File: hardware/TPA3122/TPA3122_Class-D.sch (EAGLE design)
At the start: 49 parts, among them CN1 Left_Speaker, CN2 Right_Speaker, CN3 Power_Supply, J1 SJ-3523-SMT, J4 POWER_JACKSLT, Q1 FQP47P06, U1 TPA3122D2_N_20

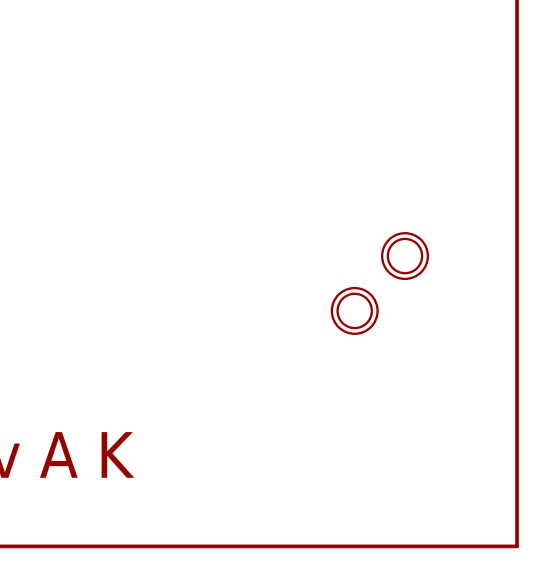
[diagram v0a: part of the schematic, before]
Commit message: Corrected TPA3122 Power Jack
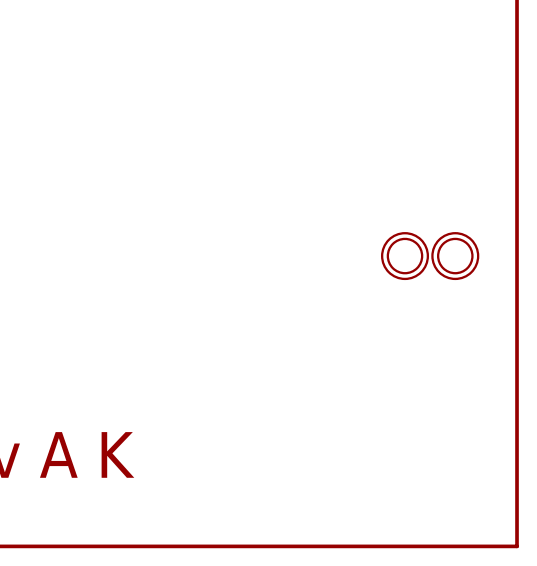
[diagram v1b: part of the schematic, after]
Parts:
- J4: device SparkFun-Connectors:POWER_JACKSLT -> TPA3122:POWER_JACKSLT
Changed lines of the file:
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@@
 <?xml version="1.0" encoding="utf-8"?>
 <!DOCTYPE eagle SYSTEM "eagle.dtd">
-<eagle version="8.4.0">
+<eagle version="8.7.1">
 <drawing>
 <settings>
@@
 <part name="ROUT" library="tlv" library_urn="urn:adsk.eagle:library:1326846" deviceset="TP" device="B2,54" package3d_urn="urn:adsk.eagle:package:1326893/1"/>
 <part name="R_FIL" library="tlv" library_urn="urn:adsk.eagle:library:1326846" deviceset="TP" device="B2,54" package3d_urn="urn:adsk.eagle:package:1326893/1"/>
-<part name="J4" library="SparkFun-Connectors" deviceset="POWER_JACK" device="SLT"/>
+<part name="J4" library="TPA3122" deviceset="POWER_JACK" device="SLT"/>
 <part name="GND9" library="SparkFun-Aesthetics" deviceset="GND" device=""/>
 <part name="J3" library="SparkFun-Connectors" library_urn="urn:adsk.eagle:library:513" deviceset="CONN_01" device="" package3d_urn="urn:adsk.eagle:package:38028/1"/>
@@
 </instance>
 <instance part="U$2" gate="G$1" x="294.894" y="-87.122"/>
-<instance part="U$3" gate="G$1" x="289.306" y="-93.218"/>
+<instance part="U$3" gate="G$1" x="300.482" y="-87.122"/>
 <instance part="S2" gate="1" x="55.88" y="106.68"/>
 <instance part="SUPPLY4" gate="1" x="68.58" y="111.76"/>
